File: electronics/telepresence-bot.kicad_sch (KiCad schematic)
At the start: 57 parts, among them J1 BATT, J19 IOLV_IN, J20 BATT_OUT, J22 PWR_GOOD, Q1 Q_PMOS, U1 LM1117DT-3.3, U13 DBG_HDR, U14 INA228, U15 SFH617A-1, U7 LM1117DT-5.0

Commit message: saving before i nuke this shit
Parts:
- removed C17, C32: 100nF, Capacitor_SMD:C_0805_2012Metric_Pad1.18x1.45mm_HandSolder, symbol Device:C
- removed C21: 100uF_10v, Capacitor_THT:CP_Radial_D6.3mm_P2.50mm, symbol Device:C
- removed C30: 100nF_10v, Capacitor_SMD:C_0805_2012Metric_Pad1.18x1.45mm_HandSolder, symbol Device:C
- removed C33: 100uF, symbol Device:C
- removed F6, F7, F8: Fuse, symbol Device:Fuse
- removed Q1: Q_PMOS, symbol Device:Q_PMOS
- removed R30, R32, R38, R39, R40, R41, R42, R43, R44, R45: 33R, symbol Device:R
- removed R34: 10k, symbol Device:R
- added C4, C6: 100nF, Capacitor_SMD:C_0805_2012Metric_Pad1.18x1.45mm_HandSolder, symbol Device:C
- added C5, C7: 100uF, Capacitor_THT:CP_Radial_D6.3mm_P2.50mm, symbol Device:C
- added D10, D11: LED, LED_THT:LED_D3.0mm, symbol Device:LED
- added F1, F2: Polyfuse, Varistor:RV_Disc_D9mm_W5.2mm_P5mm, symbol Device:Polyfuse
- added H1, H2, H3: MountingHole_Pad_MP, MountingHole:MountingHole_4.3mm_M4_ISO7380, symbol Mechanical:MountingHole_Pad_MP
- added J2: EXT_PWR_BTN, Connector_PinHeader_2.54mm:PinHeader_1x02_P2.54mm_Vertical, symbol Connector:Conn_01x02_Pin
- added Q1: Q_PMOS_GDS, Package_TO_SOT_THT:TO-220-3_Vertical, symbol Transistor_FET:Q_PMOS_GDS
- added Q3, Q4: 2N3904, Package_TO_SOT_THT:TO-92_Inline_Wide, symbol Transistor_BJT:2N3904
- added R13: 10k, Resistor_SMD:R_0805_2012Metric_Pad1.20x1.40mm_HandSolder, symbol Device:R
- added R14, R15: 1k, Resistor_THT:R_Axial_DIN0204_L3.6mm_D1.6mm_P1.90mm_Vertical, symbol Device:R
- added R4, R5, R6, R9: 0, Jumper:SolderJumper-2_P1.3mm_Open_Pad1.0x1.5mm, symbol Device:R
- added R64, R70: 470R, Resistor_THT:R_Axial_DIN0204_L3.6mm_D1.6mm_P1.90mm_Vertical, symbol Device:R
- C1: renamed from C19; value 100uF_50v -> 100uF; V (none) -> 50V
- C11: renamed from C35; footprint (none) -> Capacitor_THT:CP_Radial_D8.0mm_P5.00mm; V (none) -> 100V
- C12: renamed from C34; footprint (none) -> Capacitor_SMD:C_1206_3216Metric_Pad1.33x1.80mm_HandSolder; V (none) -> 100V
- C2: renamed from C22; value 100nF_50v -> 100nF; footprint Capacitor_SMD:C_0805_2012Metric_Pad1.18x1.45mm_HandSolder -> Capacitor_SMD:C_1206_3216Metric_Pad1.33x1.80mm_HandSolder; V (none) -> 50V
- C3: renamed from C20; value 100uF_50v -> 100uF; footprint Capacitor_SMD:C_0805_2012Metric_Pad1.18x1.45mm_HandSolder -> Capacitor_THT:CP_Radial_D6.3mm_P2.50mm; V (none) -> 10V
- C8: renamed from C29; value 100nF_10v -> 100nF; V (none) -> 10V
- C9: renamed from C27; V (none) -> 10V
- D1: renamed from D9; footprint (none) -> Diode_THT:D_DO-41_SOD81_P2.54mm_Vertical_AnodeUp
- D2: renamed from D7; footprint (none) -> LED_THT:LED_D3.0mm
- D3: renamed from D6; footprint (none) -> LED_THT:LED_D3.0mm
- D4: renamed from D10; footprint (none) -> Diode_THT:D_DO-41_SOD81_P2.54mm_Vertical_AnodeUp; V (none) -> 12V
- FB1: renamed from FB2; value FerriteBead -> FB; footprint (none) -> Inductor_SMD:L_1210_3225Metric_Pad1.42x2.65mm_HandSolder
- J1: renamed from J22; value PWR_GOOD -> STATUS; footprint (none) -> Connector_PinSocket_2.54mm:PinSocket_2x04_P2.54mm_Vertical; symbol Connector:Conn_01x04_Pin -> Connector_Generic:Conn_02x04_Odd_Even
- J3: renamed from J19; footprint (none) -> Connector_PinHeader_2.54mm:PinHeader_1x02_P2.54mm_Vertical
- J4: renamed from J1; footprint (none) -> Connector:BATT_CONNECTOR
- J5: renamed from J20; footprint (none) -> Connector_PinSocket_2.54mm:PinSocket_1x02_P2.54mm_Vertical
- R1: footprint (none) -> Resistor_SMD:R_0805_2012Metric_Pad1.20x1.40mm_HandSolder
- R10: renamed from R47; value R -> 220R; footprint (none) -> Resistor_THT:R_Axial_DIN0204_L3.6mm_D1.6mm_P1.90mm_Vertical
- R11: renamed from R49; footprint (none) -> Resistor_SMD:R_0805_2012Metric_Pad1.20x1.40mm_HandSolder
- R12: renamed from R48; footprint (none) -> Resistor_SMD:R_0805_2012Metric_Pad1.20x1.40mm_HandSolder
- R16: renamed from R3; value 1k -> 10k; footprint (none) -> Resistor_SMD:R_0805_2012Metric_Pad1.20x1.40mm_HandSolder
- R17: renamed from R5; value 1k -> 10k; footprint (none) -> Resistor_SMD:R_0805_2012Metric_Pad1.20x1.40mm_HandSolder
- R18: renamed from R31; footprint (none) -> Resistor_SMD:R_0805_2012Metric_Pad1.20x1.40mm_HandSolder
- R19: renamed from R29; footprint (none) -> Resistor_SMD:R_0805_2012Metric_Pad1.20x1.40mm_HandSolder
- R2: renamed from R36; footprint (none) -> Resistor_THT:R_Axial_DIN0204_L3.6mm_D1.6mm_P1.90mm_Vertical
- R20: renamed from R28; footprint (none) -> Resistor_SMD:R_0805_2012Metric_Pad1.20x1.40mm_HandSolder
- R21: renamed from R18; footprint (none) -> Resistor_SMD:R_0805_2012Metric_Pad1.20x1.40mm_HandSolder
- R22: renamed from R2; footprint (none) -> Resistor_SMD:R_Shunt_Vishay_WSK2512_6332Metric_T2.66mm
- R3: renamed from R33; footprint (none) -> Resistor_THT:R_Axial_DIN0204_L3.6mm_D1.6mm_P1.90mm_Vertical
- R7: renamed from R35; footprint (none) -> Resistor_SMD:R_0805_2012Metric_Pad1.20x1.40mm_HandSolder
- R8: renamed from R46; footprint (none) -> Resistor_SMD:R_0805_2012Metric_Pad1.20x1.40mm_HandSolder
- U1: renamed from U2; footprint (none) -> RF_Module:ESP32-C5-DevKitC-1-v1.2
- U2: renamed from U7; footprint Package_TO_SOT_SMD:TO-252-3_TabPin2 -> Package_TO_SOT_THT:TO-220-3_Vertical
- U3: renamed from U1; footprint Package_TO_SOT_SMD:TO-252-3_TabPin2 -> Package_TO_SOT_THT:TO-220-3_Vertical
- U5: renamed from U13; footprint (none) -> Connector_PinSocket_2.54mm:PinSocket_2x14_P2.54mm_Vertical
- renumbered U15 to U4, U14 to U6
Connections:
- net AUX_POWER_RAIL is gone; now on net AUX_PWR_RAIL: C11.1, C12.1
- net GPIO15 is gone; now on net DRIVER_CS: U1.22 (NC/GPIO15), U5.19 (GPIO15)
- net GPIO23 is gone; now on net IO_DRV_ENABLE: U1.21 (GPIO23), U5.18 (GPIO23)
- net GPIO24 is gone; now on net IO_MP_ENABLE: U1.20 (GPIO24), U5.17 (GPIO24)
- net +BATT: now also R22.1
- net 3v3_compute: now also J1.2 (Pin_2), C6.1, C7.1; no longer J1.1 (Pin_1)
- net 5v_compute: now also J1.3 (Pin_3), J1.5 (Pin_5), J1.8 (Pin_8), D10.2 (A), D11.2 (A); no longer J1.4 (Pin_4)
- net AUX_PWR_ENABLE: now also U1.24 (MTCK/GPIO4/LP_GPIO4/LP_UART_RXD/ADC1_CH3/FSPIHD), U5.21 (GPIO4)
- net AUX_PWR_RAIL: now also R12.1, F1.1, Q1.2 (D); no longer R12.2
- net BATT_ALERT: now also R7.2, U5.22 (GPIO5); no longer R7.1
- net DRIVER_CLOCK: now also R9.1
- net DRIVER_CS: no longer U1.11 (GPIO10/FSPICS0/SDIO_CMD)
- net DRIVER_SCK: now also U1.10 (GPIO9/PAD_COMP1/SDIO_CLK), R5.1; no longer U1.7 (GPIO6/LP_GPIO6/ADC1_CH5/FSPICLK), U5.8 (GPIO6)
- net DRIVER_SDI: now also U1.11 (GPIO10/FSPICS0/SDIO_CMD), R6.1; no longer U1.3 (GPIO2/MTMS/LP_GPIO2/LP_UART_RTSN/LP_I2C_SDA/ADC1_CH1/FSPIQ)
- net DRIVER_SDO: now also R4.1
- net IOLV_IN: now also F2.2
- net IO_DRV_ENABLE: now also R15.1; no longer U1.12 (GPIO26)
- net IO_MP_ENABLE: now also R14.1; no longer U1.4 (GPIO3/LP_GPIO3/MTDI/LP_UART_CTSN/LP_I2C_SCL/ADC1_CH2), U5.5 (GPIO3)
- net MOTOR_POWER_RAIL: now also D4.1 (K), R8.1, Q1.3 (S)
- net SCL: now also U1.4 (GPIO3/LP_GPIO3/MTDI/LP_UART_CTSN/LP_I2C_SCL/ADC1_CH2), U5.5 (GPIO3); no longer U1.25 (MTDO/GPIO5/LP_GPIO5/LP_UART_TXD/ADC1_CH4/FSPIWP)
- net SDA: now also U1.3 (GPIO2/MTMS/LP_GPIO2/LP_UART_RTSN/LP_I2C_SDA/ADC1_CH1/FSPIQ), U5.4 (GPIO2); no longer U1.24 (MTCK/GPIO4/LP_GPIO4/LP_UART_RXD/ADC1_CH3/FSPIHD)
- net GPIO25: now reaches U1.13 (GPIO25)
- net GPIO25: now also U5.14 (GPIO25); no longer R7.2
- net RST: now reaches U1.2 (RST)
- net RST: now also U5.26 (RST)
- net at R1.2: now also U1.9 (GPIO8/PAD_COMP0/SDIO_DATA0); no longer U1.8 (GPIO7/FSPID/SDIO_DATA1)
- net at J5.2 (Pin_2): now also F1.2
- net at D4.2 (A), R11.2, R8.2: now also Q1.1 (G), R13.1; no longer R12.1
- net at FB1.1, U3.2 (VO): now also C4.1, C5.1
- net at J3.2 (Pin_2): now also F2.1
- net at U5.12 (GPIO10): now also R6.2
- net GPIO26: now reaches U5.13 (GPIO26)
- net GPIO26: now also U1.12 (GPIO26)
- net at U5.23 (GPIO28): now also R9.2
- net GPIO7: now reaches U5.9 (GPIO7)
- net GPIO7: now also U1.8 (GPIO7/FSPID/SDIO_DATA1)
- net -BATT renamed GND
- net GND: now also J1.4 (Pin_4), J1.6 (Pin_6), R12.2, U5.27 (GND), U5.28 (GND), C4.2, C5.2, C6.2, C7.2, H1.MP, H2.MP, H3.MP, J2.1 (Pin_1), Q3.1 (E), Q4.1 (E); no longer J1.2 (Pin_2), J1.3 (Pin_3), U5.26 (GND)
- net GPIO13: no longer names the net of U1.30 (GPIO13/USBDM/SDIO_DATA3)
- net GPIO13: no longer U5.25 (GPIO13)
- net GPIO14: no longer names the net of U1.29 (GPIO14/USBDP/SDIO_DATA2)
- net GPIO14: no longer U5.24 (GPIO14)
- net GPIO8: no longer names the net of U5.10 (GPIO8)
- net GPIO8: now also R4.2; no longer U1.9 (GPIO8/PAD_COMP0/SDIO_DATA0)
- net GPIO9: no longer names the net of U5.11 (GPIO9)
- net GPIO9: now also R5.2; no longer U1.10 (GPIO9/PAD_COMP1/SDIO_CLK)
- new net: R7.1, U1.25 (MTDO/GPIO5/LP_GPIO5/LP_UART_TXD/ADC1_CH4/FSPIWP)
- new net: Q3.2 (B), R14.2
- new net: J1.7 (Pin_7), Q3.3 (C), R64.2
- new net: J2.2 (Pin_2), R13.2
- new net: J1.1 (Pin_1), Q4.3 (C), R70.1
- new net: Q4.2 (B), R15.2
- new net: D11.1 (K), R70.2
- new net: D10.1 (K), R64.1
- new net GPIO6: U1.7 (GPIO6/LP_GPIO6/ADC1_CH5/FSPICLK), U5.8 (GPIO6)
- no-connect marks 1 -> 4
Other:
- moved on the sheet: C11, C12, C9, D2, D3, D4, J4, J5, R1, R11, R12, R16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

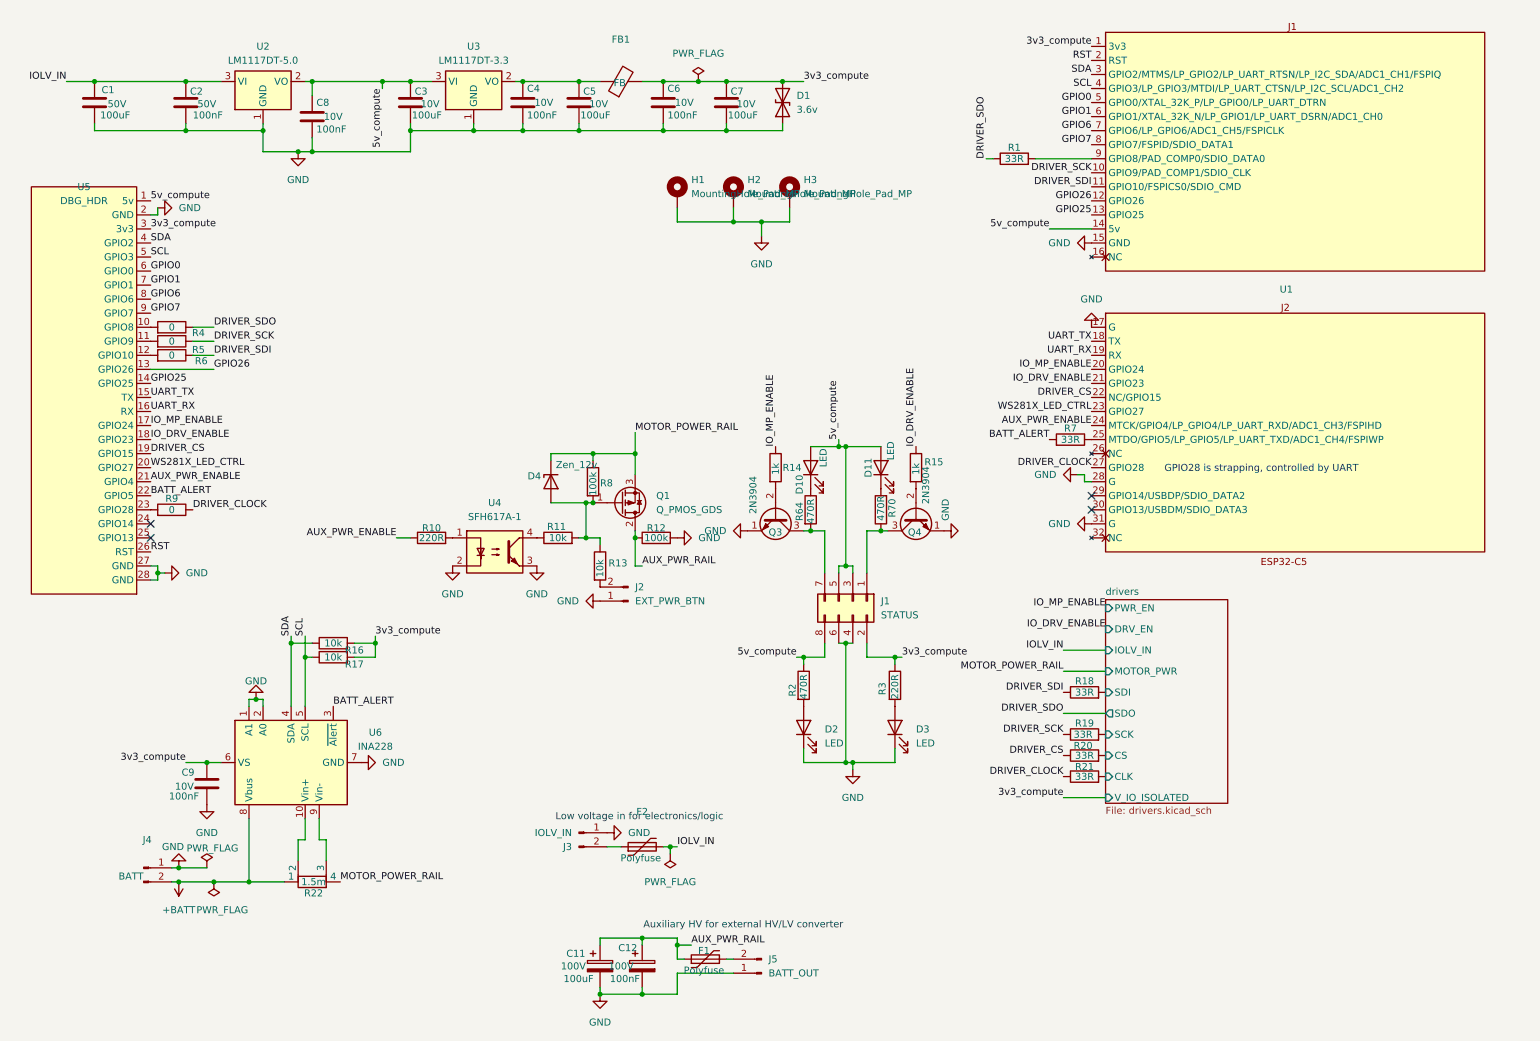
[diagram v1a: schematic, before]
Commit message: Switching to a bigger PCB since cost seems negligible
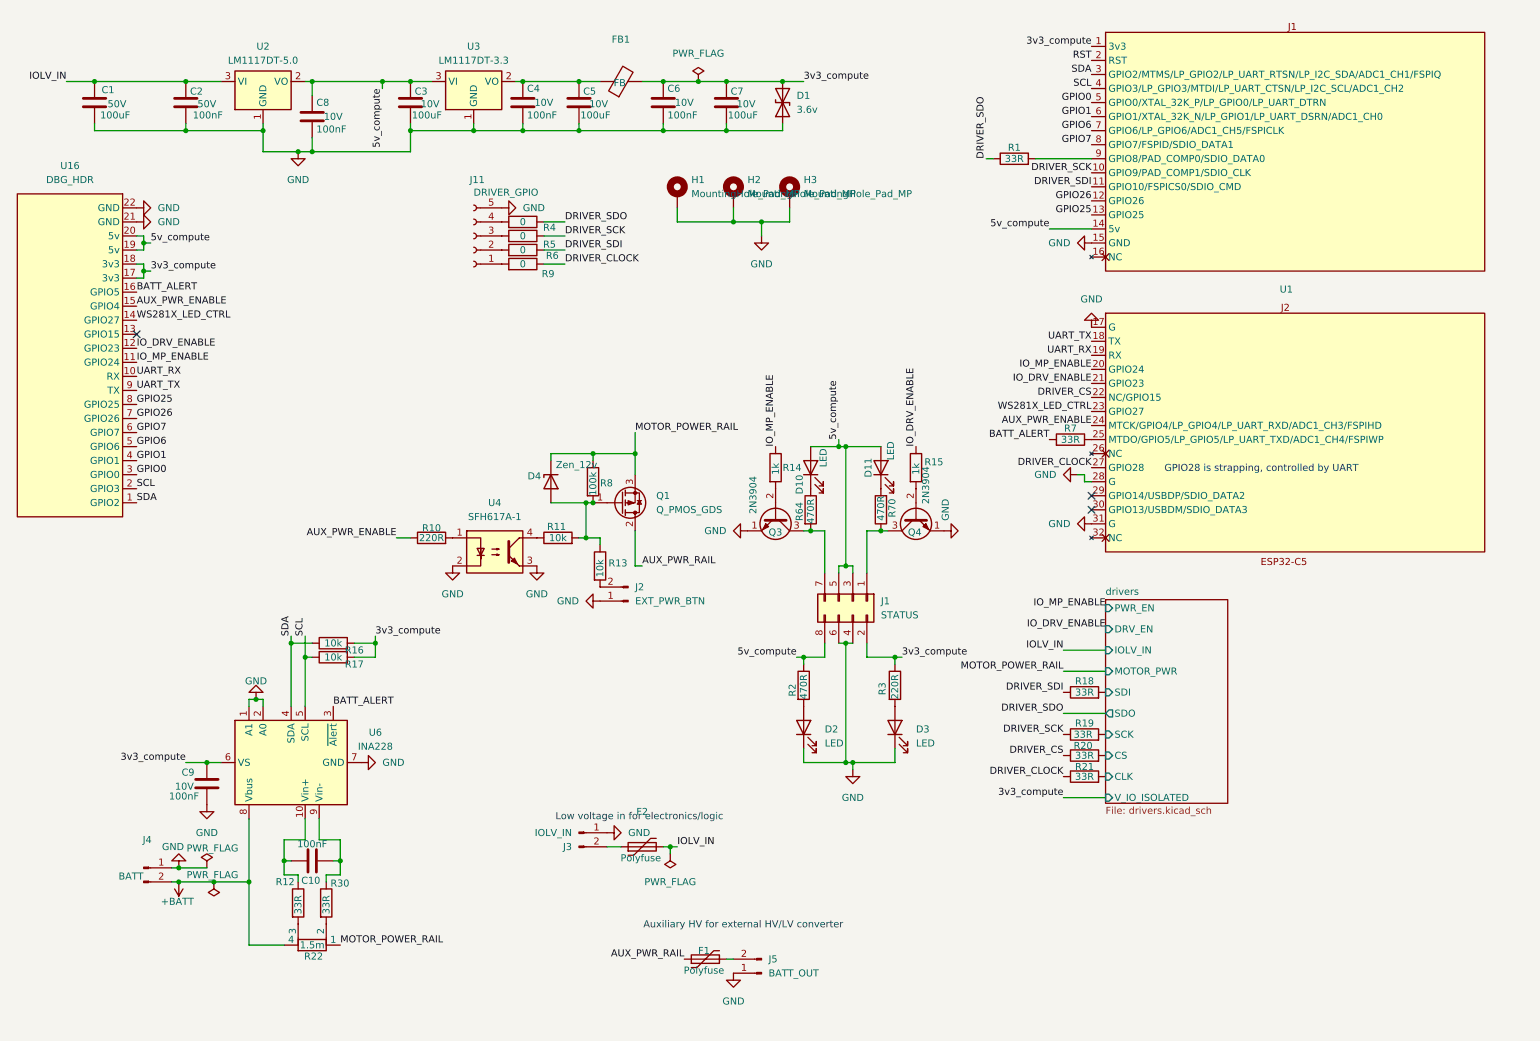
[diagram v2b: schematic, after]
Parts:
- removed C11: 100uF, Capacitor_THT:CP_Radial_D8.0mm_P5.00mm, symbol Device:C_Polarized
- removed C12: 100nF, Capacitor_SMD:C_1206_3216Metric_Pad1.33x1.80mm_HandSolder, symbol Device:C_Polarized
- removed U5: DBG_HDR, Connector_PinSocket_2.54mm:PinSocket_2x14_P2.54mm_Vertical, symbol Connector:DBG_GPIO
- added C10: 100nF, Capacitor_SMD:C_1206_3216Metric_Pad1.33x1.80mm_HandSolder, symbol Device:C
- added J11: DRIVER_GPIO, Connector_PinSocket_2.54mm:PinSocket_1x05_P2.54mm_Vertical, symbol Connector:Conn_01x05_Socket
- added R30: 33R, Resistor_SMD:R_0805_2012Metric_Pad1.20x1.40mm_HandSolder, symbol Device:R
- added U16: DBG_HDR, Connector_PinSocket_2.54mm:PinSocket_2x11_P2.54mm_Vertical, symbol Connector:DBG_GPIO
- R12: value 100k -> 33R
- R22: footprint Resistor_SMD:R_Shunt_Vishay_WSK2512_6332Metric_T2.66mm -> Resistor_SMD:R_Shunt_Vishay_WSKW0612
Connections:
- net +BATT: now also R22.4; no longer R22.1
- net 3v3_compute: now also U16.17 (3v3), U16.18 (3v3)
- net 5v_compute: now also U16.19 (5v), U16.20 (5v)
- net AUX_PWR_ENABLE: now also U16.15 (GPIO4)
- net AUX_PWR_RAIL: no longer R12.1
- net BATT_ALERT: now also U16.16 (GPIO5)
- net GND: now also J11.5 (Pin_5), U16.21 (GND), U16.22 (GND); no longer R12.2
- net GPIO0: now also U16.3 (GPIO0)
- net GPIO1: now also U16.4 (GPIO1)
- net GPIO25: now also U16.8 (GPIO25)
- net GPIO26: now also U16.7 (GPIO26)
- net GPIO6: now also U16.5 (GPIO6)
- net GPIO7: now also U16.6 (GPIO7)
- net IO_DRV_ENABLE: now also U16.12 (GPIO23)
- net IO_MP_ENABLE: now also U16.11 (GPIO24)
- net MOTOR_POWER_RAIL: now also R22.1; no longer R22.4
- net SCL: now also U16.2 (GPIO3)
- net SDA: now also U16.1 (GPIO2)
- net UART_RX: now also U16.10 (RX)
- net UART_TX: now also U16.9 (TX)
- net WS281X_LED_CTRL: now also U16.14 (GPIO27)
- net at R9.2: now also J11.1 (Pin_1)
- net at R6.2: now also J11.2 (Pin_2)
- net at U6.10 (Vin+): now also R12.1, C10.1; no longer R22.2
- net at R22.3: now also R12.2; no longer U6.9 (Vin-)
- net at R4.2: now also J11.4 (Pin_4)
- net at R5.2: now also J11.3 (Pin_3)
- new net: R22.2, R30.2
- new net: C10.2, R30.1, U6.9 (Vin-)
- no-connect marks 4 -> 3
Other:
- moved on the sheet: R22, R4, R5, R6, R9

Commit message: Updating electronics CAD post-production
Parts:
- added C12: 100nF, Capacitor_SMD:C_0805_2012Metric_Pad1.18x1.45mm_HandSolder, symbol Device:C
- added D12: D_Schottky, Diode_THT:D_DO-201AD_P5.08mm_Vertical_KathodeUp, symbol Device:D_Schottky
- added H4: MountingHole_Pad_MP, MountingHole:MountingHole_4.3mm_M4_ISO7380, symbol Mechanical:MountingHole_Pad_MP
- added JP1, JP2: Jumper_2_Bridged, Connector_PinSocket_2.54mm:PinSocket_1x02_P2.54mm_Vertical, symbol Jumper:Jumper_2_Bridged
- C1, C3, C5, C7: symbol Device:C -> Device:C_Polarized
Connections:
- net 3v3_compute: now also C12.2, JP1.1 (A); no longer U1.1 (3v3)
- net 5v_compute: now also JP2.1 (A); no longer U1.14 (5v)
- net GND: now also C12.1, H4.MP
- net IOLV_IN: now also D12.2 (A); no longer C1.1, C2.1, U2.3 (VI)
- new net: JP1.2 (B), U1.1 (3v3)
- new net: JP2.2 (B), U1.14 (5v)
- new net: C1.1, C2.1, D12.1 (K), U2.3 (VI)
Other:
- moved on the sheet: F1

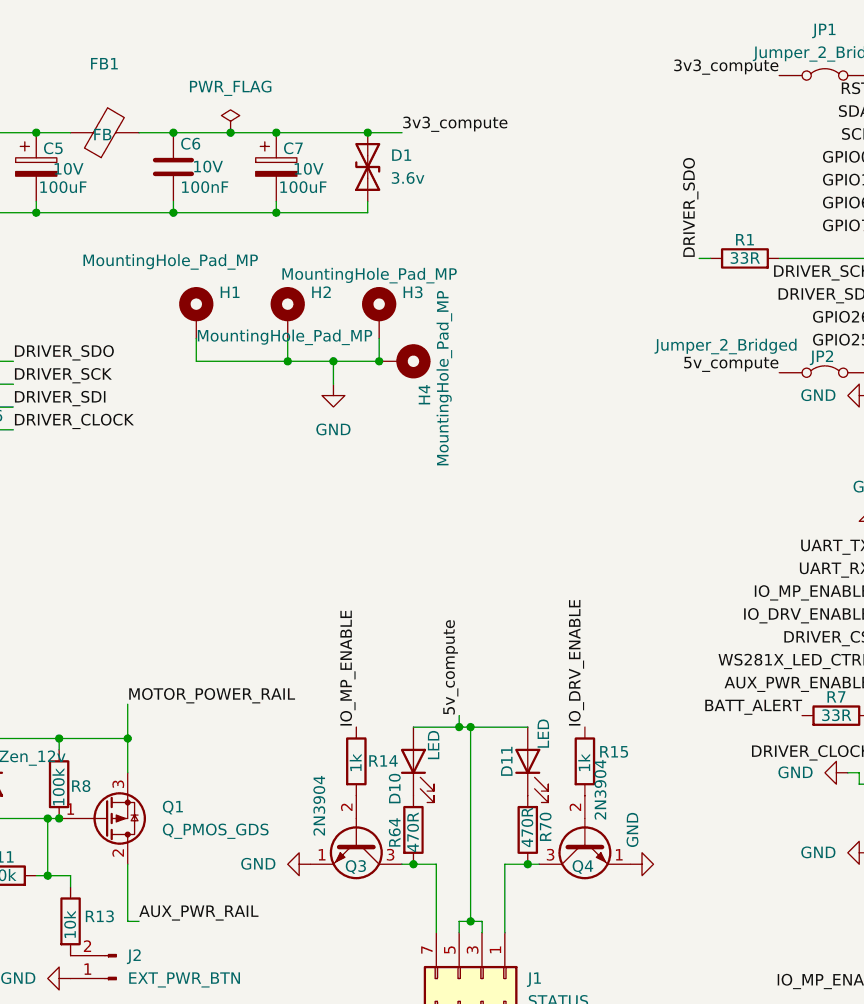
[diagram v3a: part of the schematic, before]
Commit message: Some vibe coding to set up project structure. Almost all of the code will be rewritten to my standards
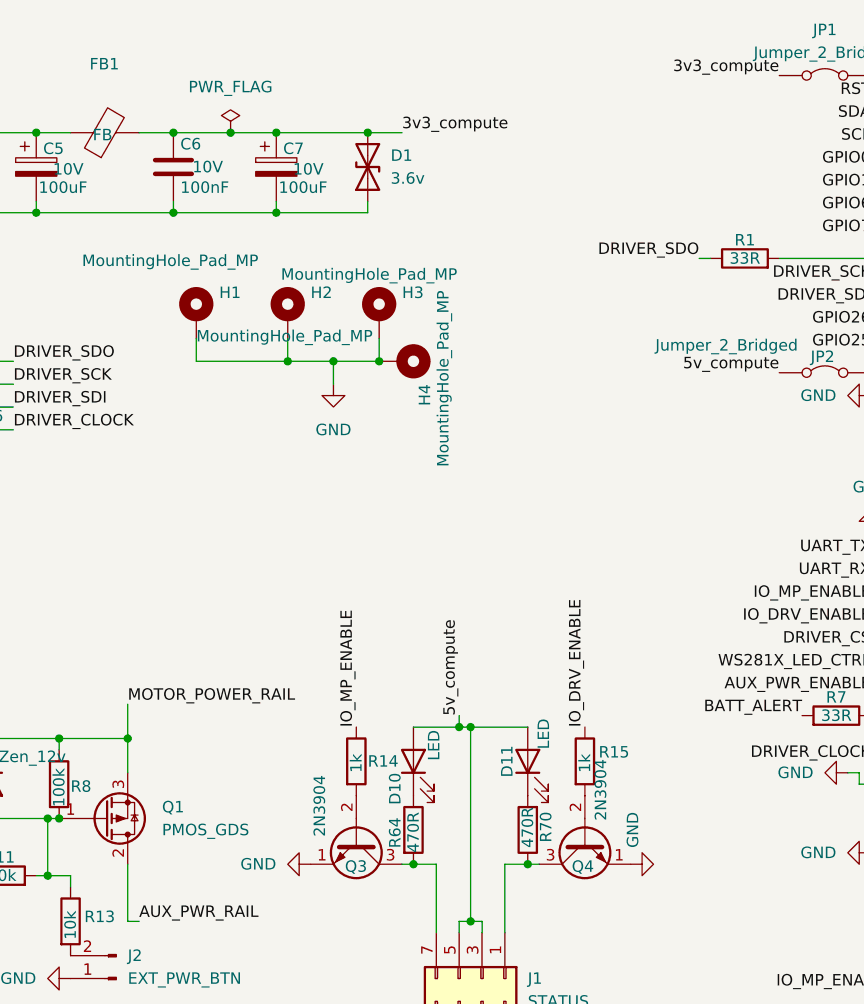
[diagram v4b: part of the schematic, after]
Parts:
- C1, C3, C5, C7, D10, D11, D2, D3, U2, U3, U4: msrcrt (none) -> Y
- C10, C12, C2, C4, C6, C8, C9, D1, FB1, J1, J11, J2, J3, J4, J5, Q3, Q4, R1, R10, R11, R12, R13, R14, R15, R16, R17, R18, R19, R2, R20, R21, R22, R3, R30, R4, R5, R6, R64, R7, R70, R8, R9, U1, U6: msrcrt (none) -> NA
- D12, D4, F1, F2, JP1, JP2: msrcrt (none) -> N
- Q1: value Q_PMOS_GDS -> PMOS_GDS; msrcrt (none) -> Y
